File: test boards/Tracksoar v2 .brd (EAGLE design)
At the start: 50.4 x 19.6 mm, 48 parts, among them IC1 BME280, IC2 74AHC1G125DBV, Y1 16MHZ

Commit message: updated thermal pads
updated thermal pads
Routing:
- net GND: vias 87 -> 91
- removed copper zone on layer 1, net THERM
- removed copper zone on layer 16, net THERM
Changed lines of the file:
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@@
 <wire x1="27.2584" y1="17.2762" x2="27.5336" y2="17.5514" width="0.8128" layer="16"/>
 <wire x1="27.5336" y1="17.5514" x2="28.2878" y2="17.5514" width="0.8128" layer="16"/>
+<polygon width="0.1524" layer="16" isolate="0.254" rank="2">
+<vertex x="26.6954" y="19.6342"/>
+<vertex x="31.5722" y="19.6088"/>
+<vertex x="31.5722" y="15.0876"/>
+<vertex x="26.6954" y="15.113"/>
+</polygon>
+<polygon width="0.1524" layer="1" isolate="0.254" thermals="no" rank="3">
+<vertex x="26.6954" y="19.6342"/>
+<vertex x="31.5722" y="19.6088"/>
+<vertex x="31.5722" y="15.113"/>
+<vertex x="31.5976" y="15.0876"/>
+<vertex x="26.6954" y="15.113"/>
+</polygon>
+<via x="27.2034" y="15.7988" extent="1-16" drill="0.2"/>
+<via x="29.083" y="16.129" extent="1-16" drill="0.2"/>
+<via x="29.4132" y="17.526" extent="1-16" drill="0.2"/>
+<via x="30.861" y="17.5514" extent="1-16" drill="0.2"/>
 </signal>
 <signal name="VCC">
@@
 <wire x1="16.64174375" y1="6.53254375" x2="16.64174375" y2="6.540728125" width="0.3048" layer="16"/>
 </signal>
-<signal name="THERM">
-<polygon width="0.1524" layer="1" isolate="0.254" thermals="no" rank="3">
-<vertex x="26.6954" y="19.6342"/>
-<vertex x="31.5722" y="19.6088"/>
-<vertex x="31.5722" y="15.113"/>
-<vertex x="31.5976" y="15.0876"/>
-<vertex x="26.6954" y="15.113"/>
-</polygon>
-<polygon width="0.1524" layer="16" isolate="0.254" rank="2">
-<vertex x="26.6954" y="19.6342"/>
-<vertex x="31.5722" y="19.6088"/>
-<vertex x="31.5722" y="15.0876"/>
-<vertex x="26.6954" y="15.113"/>
-</polygon>
-</signal>
-<signal name="N$18">
-<via x="27.2034" y="15.7988" extent="1-16" drill="0.2"/>
-</signal>
-<signal name="N$21">
-<via x="29.083" y="16.129" extent="1-16" drill="0.2"/>
-</signal>
-<signal name="N$22">
-<via x="30.861" y="17.5514" extent="1-16" drill="0.2"/>
-</signal>
-<signal name="N$23">
-<via x="29.4132" y="17.526" extent="1-16" drill="0.2"/>
-</signal>
 </signals>

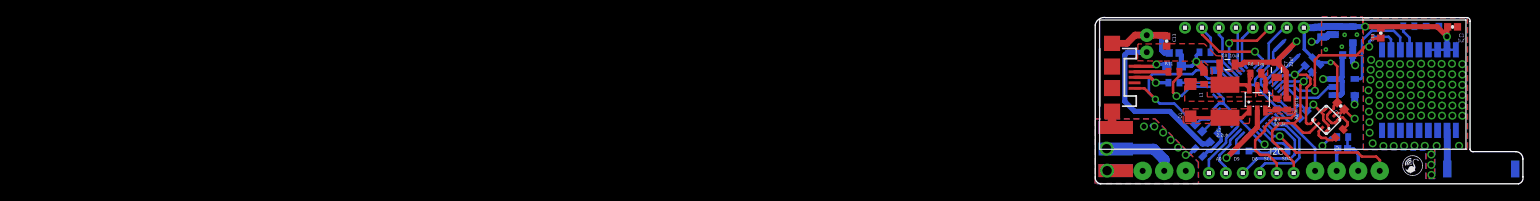
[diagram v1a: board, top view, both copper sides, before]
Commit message: removed ldo and level shifter
replaced the 3v ldo with a switching regulator, replaced level shifter with resistor dividers.
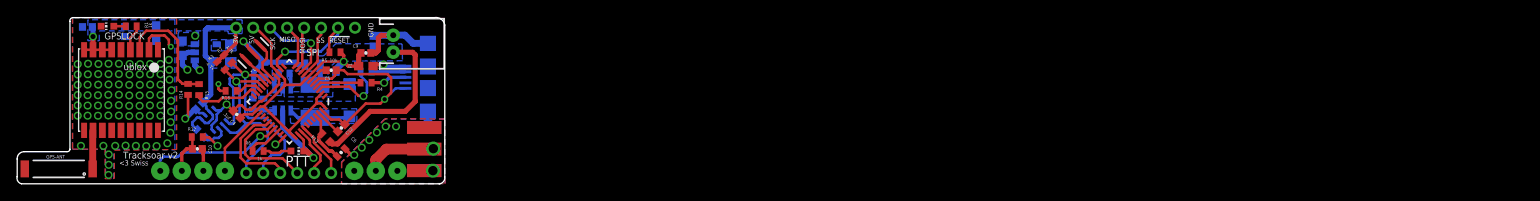
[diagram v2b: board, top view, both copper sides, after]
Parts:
- removed C2, C3: .1uf, SparkFun-Capacitors:0402-CAP
- removed IC2: 74AHC1G125DBV, 74xx-little-us:SOT23-5
- removed LM3480: LM3480IM4, SparkFun-PowerIC:SOT23-3
- added C15, C16: 10uF, SparkFun-Capacitors:0603
- added R14: 4.7k, adafruit:R0402
- added R15, R16: 10k, adafruit:R0402
- added U$5: PAM2305, PAM2305-33:DBV_R-PDSO-G5
- added U$6: 4.7uH, Nordic_nRF:RESC0805_N
- R1: value 100ohm -> 1k
- R6: value 330ohm -> 1k
- moved GPS-ANT 167.6 mm to (-122.1, 1.73), flipped to the top
- moved C1 160.9 mm to (-118.7, 18.5), flipped to the bottom
- moved GPSLOCK 156.2 mm to (-116.4, 18.5), flipped to the top
- moved U$1 153.1 mm to (-114.8, 10.8), flipped to the top
- moved R1 150.6 mm to (-113.6, 18.5), flipped to the top
- moved C11 148.0 mm to (-114.3, 17.9), flipped to the bottom
- moved C10 135.0 mm to (-105.8, 4.09), flipped to the top
- moved R12 135.0 mm to (-105.8, 5.49), flipped to the top
- moved C14 134.5 mm to (-105.6, 9.14), flipped to the bottom
- moved R2 134.2 mm to (-105.4, 5.92), flipped to the bottom
- moved IC1 131.1 mm to (-103.9, 7.52), flipped to the bottom
- moved R3 129.0 mm to (-103.0, 13.9), flipped to the top
- moved R7 127.4 mm to (-102.2, 14.7), flipped to the top
- moved C4 125.7 mm to (-101.1, 8.15), flipped to the top
- moved R10 121.9 mm to (-99.3, 9.37), flipped to the bottom
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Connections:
- new net N$18: U$5.4, U$6.1
- new net RX1: R16.2, U$1.2_TXD1
- net 3V: now also C15.1, U$5.5, U$6.2; no longer C2.2, LM3480.1
- net GND: now also C15.2, C16.2, R14.2, U$5.2; no longer C2.1, C3.1, IC2.1, IC2.3, LM3480.3
- net RX: now also R16.1; no longer U$1.2_TXD1
- net TX: now also R15.2; no longer IC2.2
- net TX1: now also R14.1, R15.1; no longer IC2.4
- net VCC: now also C16.1, U$5.1, U$5.3; no longer C3.2, IC2.5, LM3480.2
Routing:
- net RX: track 20.0 -> 3.22 mm, vias 2 -> 0
- net RX1: track 0.00 -> 14.2 mm, vias 0 -> 2
- net 3V: track 43.7 -> 31.8 mm, vias 3 -> 1
- net GND: track 101.8 -> 95.9 mm, vias 91 -> 86
- net VCC: track 51.1 -> 47.3 mm
- net TX1: track 12.1 -> 14.0 mm
- net TX: track 6.95 -> 8.03 mm
- net SCL: track 29.5 -> 30.0 mm
- added copper zone on layer 16, net 3V
- added copper zone on layer 16, net N$12
- added copper zone on layer 16, net N$13
- added copper zone on layer 16, net N$18
- added copper zone on layer 16, net N$19
- added copper zone on layer 16, net N$9
- added copper zone on layer 16, net VCC
- added copper zone on layer 16, net VIN
- removed copper zone on layer 1, net N$12
- removed copper zone on layer 1, net N$13
- removed copper zone on layer 1, net N$19
- removed copper zone on layer 1, net N$9
- removed copper zone on layer 1, net VIN
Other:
- outline, holes or cut-outs redrawn
- board text removed: "74AHC1G125"

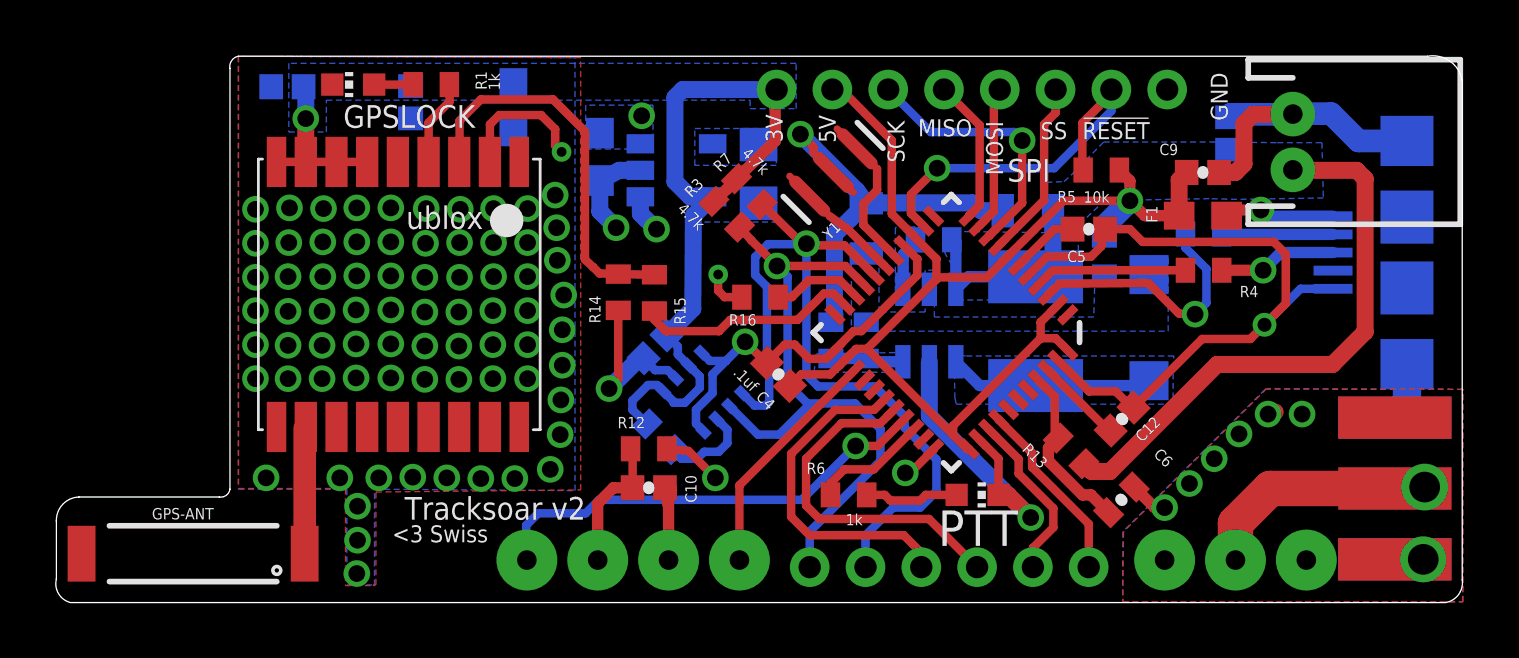
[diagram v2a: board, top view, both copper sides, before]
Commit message: updated rf paths
seperated RF GND from GND and coupled via an inductor. Implemented path cleanups. Made all RF impedence matched.
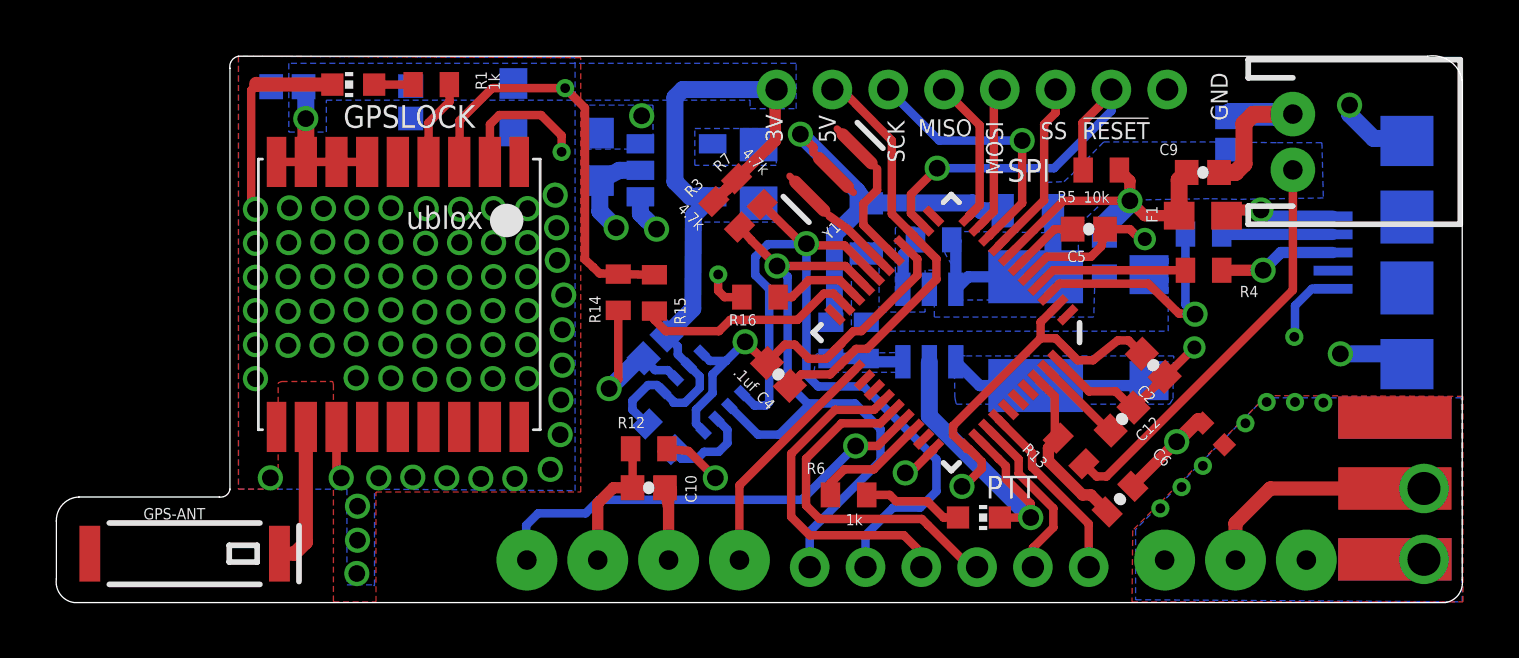
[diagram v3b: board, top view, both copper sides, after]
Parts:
- added C2: .1uf, SparkFun-Capacitors:0402-CAP
- added U$7: (no value), Nordic_nRF:RESC0402_N
- GPS-ANT: value ANTENNA2SMD3 -> 1.575GHz; device SparkFun-RF:ANTENNA-CHIP4 -> SparkFun-GPS:ANT-GPS-2X7MM
- U$4: value ATMEGA32U4QFN2 -> ATMEGA32U4
- moved PTT 0.81 mm to (-94.0, 3.02)
- moved GPS-ANT 0.30 mm to (-122.4, 1.73)
- moved C6 0.06 mm to (-88.9, 3.68)
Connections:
- new net RFGND: J$1.GND@0, J$1.GND@1, J$1.GND@2, J$1.GND@3, U$2.RFGND, U$2.RFGND2, U$7.2
- net GND: now also C2.1, U$7.1; no longer J$1.GND@0, J$1.GND@1, J$1.GND@2, J$1.GND@3, U$2.RFGND, U$2.RFGND2
- net N$6: now also GPS-ANT.1; no longer GPS-ANT.SIG
- net VCC: now also C2.2
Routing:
- net VIN: track 28.0 -> 22.3 mm
- net VCC: track 47.3 -> 45.2 mm, vias 3 -> 4
- net N$1: track 8.67 -> 9.74 mm, vias 1 -> 0
- net TX1: track 14.0 -> 14.9 mm, vias 0 -> 1
- net N$6: track 4.56 -> 5.31 mm
- net RFGND: track 0.00 -> 0.61 mm, vias 0 -> 8
- net GND: track 95.9 -> 95.5 mm, vias 86 -> 82
- added copper zone on layer 1, net RFGND
- added copper zone on layer 16, net RFGND
- added copper zone on layer 2, net RFGND
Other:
- outline, holes or cut-outs redrawn

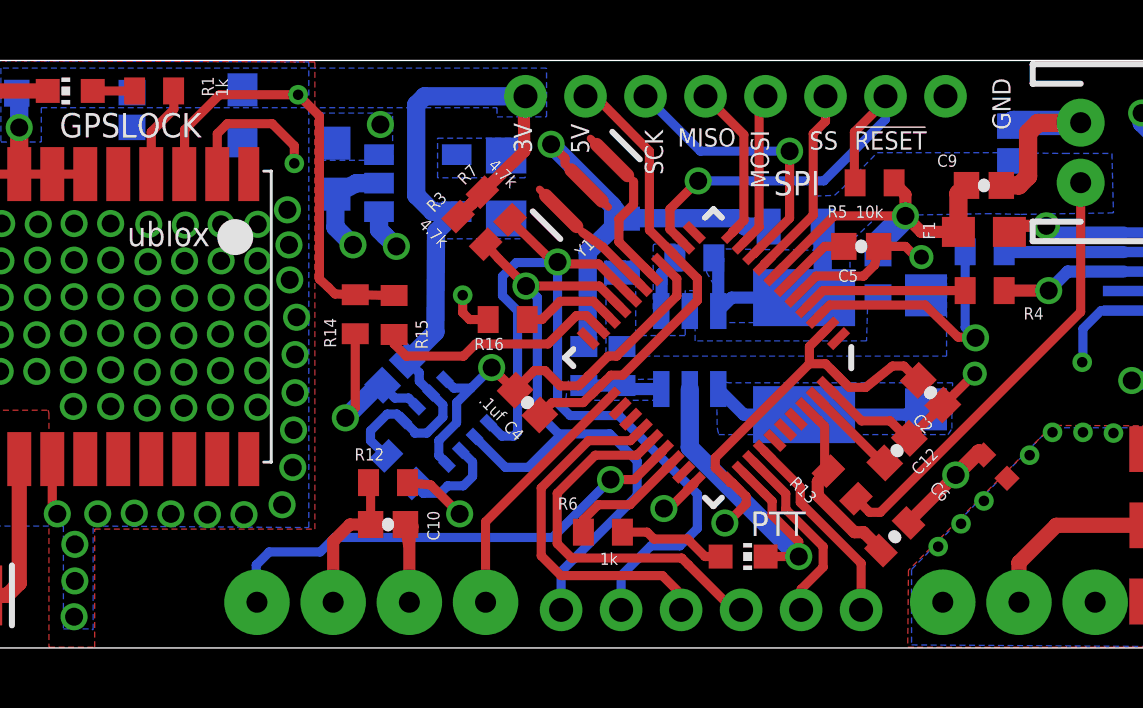
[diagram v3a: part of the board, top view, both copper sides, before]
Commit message: moved gpio header
moved the gpioheader to better center it
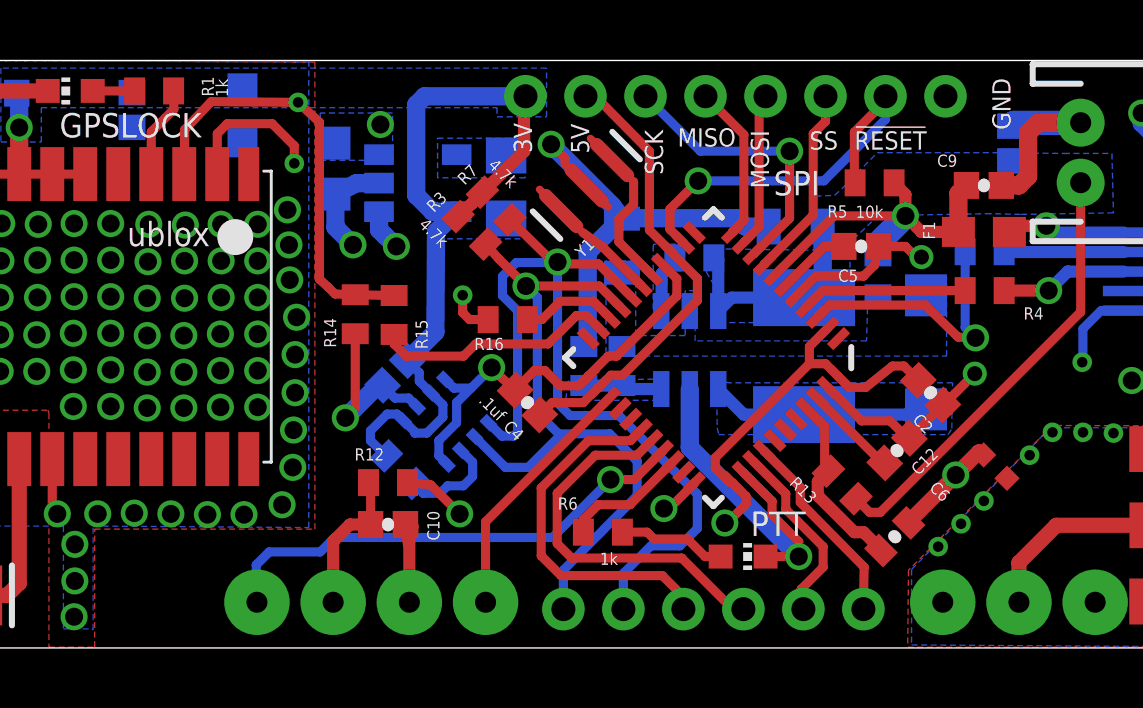
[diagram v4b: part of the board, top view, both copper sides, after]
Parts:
- moved U$3 0.08 mm to (-94.9, 1.27)
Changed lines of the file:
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@@
 <attribute name="VALUE" x="-89.1413" y="12.5984" size="0.4064" layer="27" rot="R180"/>
 </element>
-<element name="U$3" library="headers(2mm)" package="1X6" value="1X6" x="-95.0214" y="1.2446" rot="MR0"/>
+<element name="U$3" library="headers(2mm)" package="1X6" value="1X6" x="-94.9452" y="1.27" rot="MR0"/>
 <element name="L1" library="inductors" package="0402" value="BLM15HB121SN1" x="-89.4588" y="12.3952" smashed="yes" rot="MR90">
 <attribute name="NAME" x="-89.281" y="10.16" size="0.4064" layer="26" rot="MR90"/>
@@
 <via x="-86.868" y="5.7404" extent="1-16" drill="0.6"/>
 <wire x1="-88.440378125" y1="4.14261875" x2="-88.389578125" y2="4.218821875" width="0.4064" layer="1"/>
-<wire x1="-88.389578125" y1="4.218821875" x2="-86.868" y2="5.7404" width="0.4064" layer="1"/>
+<wire x1="-88.389578125" y1="4.218821875" x2="-86.868" y2="5.7404" width="0.508" layer="1"/>
 <via x="-81.0006" y="8.89" extent="1-16" drill="0.6"/>
 <wire x1="-78.613" y1="8.5222" x2="-78.9808" y2="8.89" width="0.508" layer="16"/>
@@
 <vertex x="-101.2444" y="13.6144"/>
 </polygon>
-<polygon width="0.3048" layer="16" thermals="no" rank="3">
+<polygon width="0.3048" layer="16" isolate="0.3048" thermals="no" rank="3">
 <vertex x="-100.5078" y="19.304"/>
 <vertex x="-118.6942" y="19.304"/>
@@
 <wire x1="-106.8832" y1="11.7498" x2="-107.5586" y2="11.7752" width="0.3048" layer="1"/>
 <wire x1="-107.5586" y1="11.7752" x2="-107.7824" y2="11.999" width="0.3048" layer="1"/>
-<via x="-108.7882" y="18.415" extent="1-16" drill="0.35" alwaysstop="yes"/>
-<wire x1="-111.4044" y1="18.415" x2="-108.7882" y2="18.415" width="0.3048" layer="1"/>
-<wire x1="-112.5728" y1="17.2466" x2="-111.4044" y2="18.415" width="0.3048" layer="1"/>
-<wire x1="-108.7882" y1="18.415" x2="-108.077" y2="17.7038" width="0.3048" layer="1"/>
-<wire x1="-108.077" y1="17.7038" x2="-108.077" y2="12.2682" width="0.3048" layer="1"/>
+<via x="-108.7882" y="18.161" extent="1-16" drill="0.35" alwaysstop="yes"/>
+<wire x1="-111.6838" y1="18.1864" x2="-108.7882" y2="18.161" width="0.3048" layer="1"/>
+<wire x1="-112.5728" y1="17.2466" x2="-111.6838" y2="18.1864" width="0.3048" layer="1"/>
+<wire x1="-108.7882" y1="18.161" x2="-108.077" y2="17.5006" width="0.3048" layer="1"/>
+<wire x1="-108.077" y1="17.5006" x2="-108.077" y2="12.2682" width="0.3048" layer="1"/>
 </signal>
 <signal name="VDDD">
@@
 <wire x1="-98.3996" y1="7.112" x2="-97.4852" y2="6.1976" width="0.3048" layer="16"/>
 <wire x1="-97.4852" y1="6.1976" x2="-97.4852" y2="5.0546" width="0.3048" layer="16"/>
-<wire x1="-97.4852" y1="5.0546" x2="-100.0214" y2="2.5184" width="0.3048" layer="16"/>
+<wire x1="-97.4852" y1="5.0546" x2="-99.9452" y2="2.5692" width="0.3048" layer="16"/>
 <contactref element="U$3" pad="6"/>
-<wire x1="-100.0214" y1="2.5184" x2="-100.0214" y2="1.2446" width="0.3048" layer="16"/>
+<wire x1="-99.9452" y1="2.5692" x2="-99.9452" y2="1.27" width="0.3048" layer="16"/>
 <wire x1="-102.90600625" y1="7.023425" x2="-101.876978125" y2="5.9944" width="0.3048" layer="16"/>
 <wire x1="-101.876978125" y1="5.9944" x2="-101.1174" y2="5.9944" width="0.3048" layer="16"/>
@@
 <wire x1="-95.4786" y1="3.9624" x2="-96.0628" y2="3.3782" width="0.3048" layer="16"/>
 <wire x1="-96.0628" y1="3.3782" x2="-97.028" y2="3.3782" width="0.3048" layer="16"/>
-<wire x1="-97.028" y1="3.3782" x2="-98.0214" y2="2.3848" width="0.3048" layer="16"/>
-<wire x1="-98.0214" y1="2.3848" x2="-98.0214" y2="1.2446" width="0.3048" layer="16"/>
+<wire x1="-97.028" y1="3.3782" x2="-97.9452" y2="2.461" width="0.3048" layer="16"/>
+<wire x1="-97.9452" y1="2.461" x2="-97.9452" y2="1.27" width="0.3048" layer="16"/>
 <wire x1="-101.9762" y1="11.71543125" x2="-101.9762" y2="12.36376875" width="0.3048" layer="16"/>
 <wire x1="-101.9762" y1="12.36376875" x2="-101.51776875" y2="12.8222" width="0.3048" layer="16"/>
@@
 <wire x1="-100.0252" y1="2.3876" x2="-96.647" y2="2.3876" width="0.3048" layer="1"/>
 <wire x1="-96.647" y1="2.3876" x2="-96.0214" y2="1.762" width="0.3048" layer="1"/>
-<wire x1="-96.0214" y1="1.762" x2="-96.0214" y2="1.2446" width="0.3048" layer="1"/>
+<wire x1="-96.0214" y1="1.762" x2="-95.9452" y2="1.27" width="0.3048" layer="1"/>
 </signal>
 <signal name="D9">
@@
 <contactref element="U$3" pad="3"/>
 <wire x1="-99.6696" y1="2.9718" x2="-96.0026" y2="2.9718" width="0.3048" layer="1"/>
-<wire x1="-96.0026" y1="2.9718" x2="-95.7787" y2="2.7479" width="0.3048" layer="1"/>
-<wire x1="-95.7787" y1="2.7479" x2="-94.2754" y2="1.2446" width="0.3048" layer="1"/>
-<wire x1="-94.2754" y1="1.2446" x2="-94.0214" y2="1.2446" width="0.3048" layer="1"/>
+<wire x1="-96.0026" y1="2.9718" x2="-94.2754" y2="1.2446" width="0.3048" layer="1"/>
+<wire x1="-94.2754" y1="1.2446" x2="-93.9452" y2="1.27" width="0.3048" layer="1"/>
 </signal>
 <signal name="D13">
@@
 <wire x1="-91.2876" y1="3.3528" x2="-91.2876" y2="2.667" width="0.3048" layer="1"/>
 <wire x1="-91.2876" y1="2.667" x2="-92.0214" y2="1.9332" width="0.3048" layer="1"/>
-<wire x1="-92.0214" y1="1.9332" x2="-92.0214" y2="1.2446" width="0.3048" layer="1"/>
+<wire x1="-92.0214" y1="1.9332" x2="-91.9452" y2="1.27" width="0.3048" layer="1"/>
 </signal>
 <signal name="N$19">
@@
 <contactref element="U$3" pad="1"/>
 <contactref element="U$4" pad="37"/>
-<wire x1="-90.0214" y1="1.2446" x2="-90.0214" y2="2.7978" width="0.3048" layer="1"/>
-<wire x1="-90.0214" y1="2.7978" x2="-92.0496" y2="4.826" width="0.3048" layer="1"/>
+<wire x1="-89.9452" y1="1.27" x2="-89.9198" y2="2.6708" width="0.3048" layer="1"/>
+<wire x1="-89.9198" y1="2.6708" x2="-92.0496" y2="4.826" width="0.3048" layer="1"/>
 <wire x1="-92.0496" y1="4.826" x2="-92.0496" y2="5.334" width="0.3048" layer="1"/>
 <wire x1="-92.0496" y1="5.334" x2="-93.24814375" y2="6.53254375" width="0.3048" layer="1"/>
